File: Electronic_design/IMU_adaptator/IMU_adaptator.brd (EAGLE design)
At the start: 47.7 x 34.1 mm, 5 parts, among them J1 CLM-110-02-XX-D

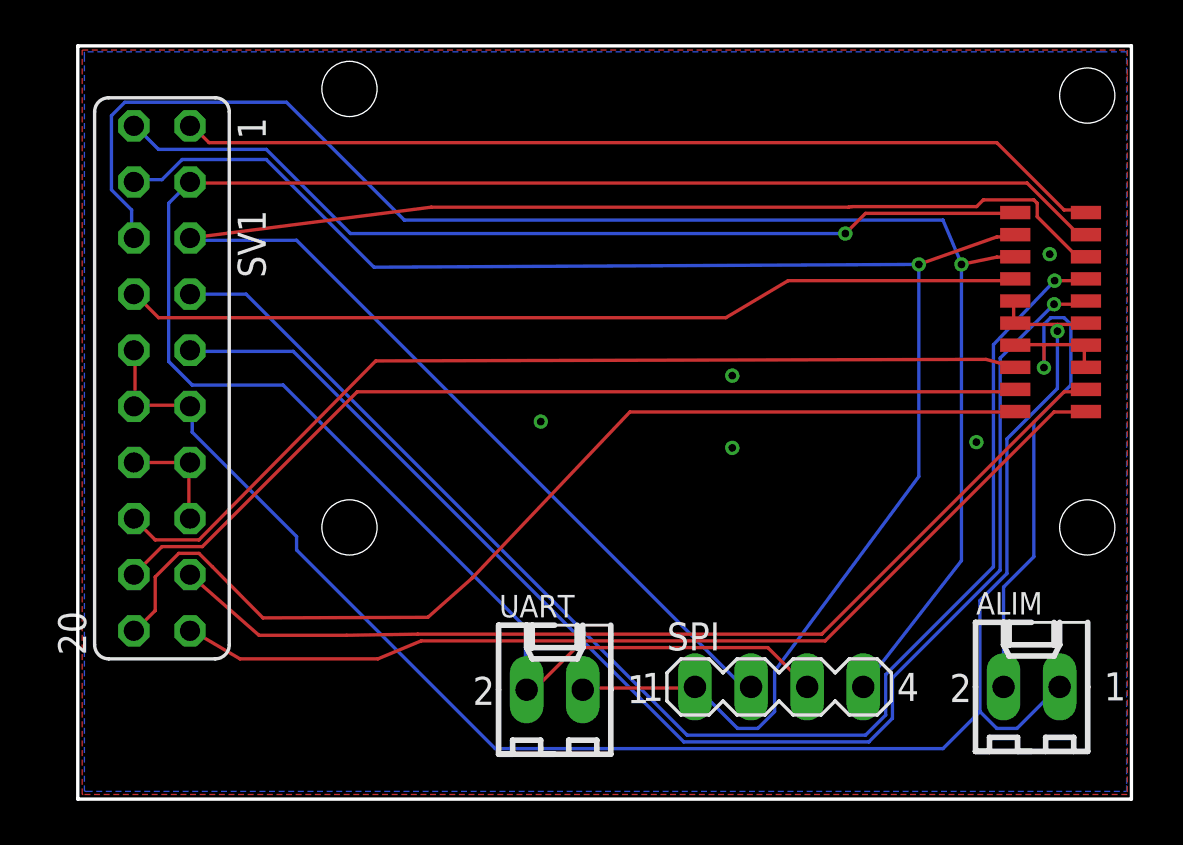
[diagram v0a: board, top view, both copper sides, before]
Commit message: reroutage carte IMU et STEPPER
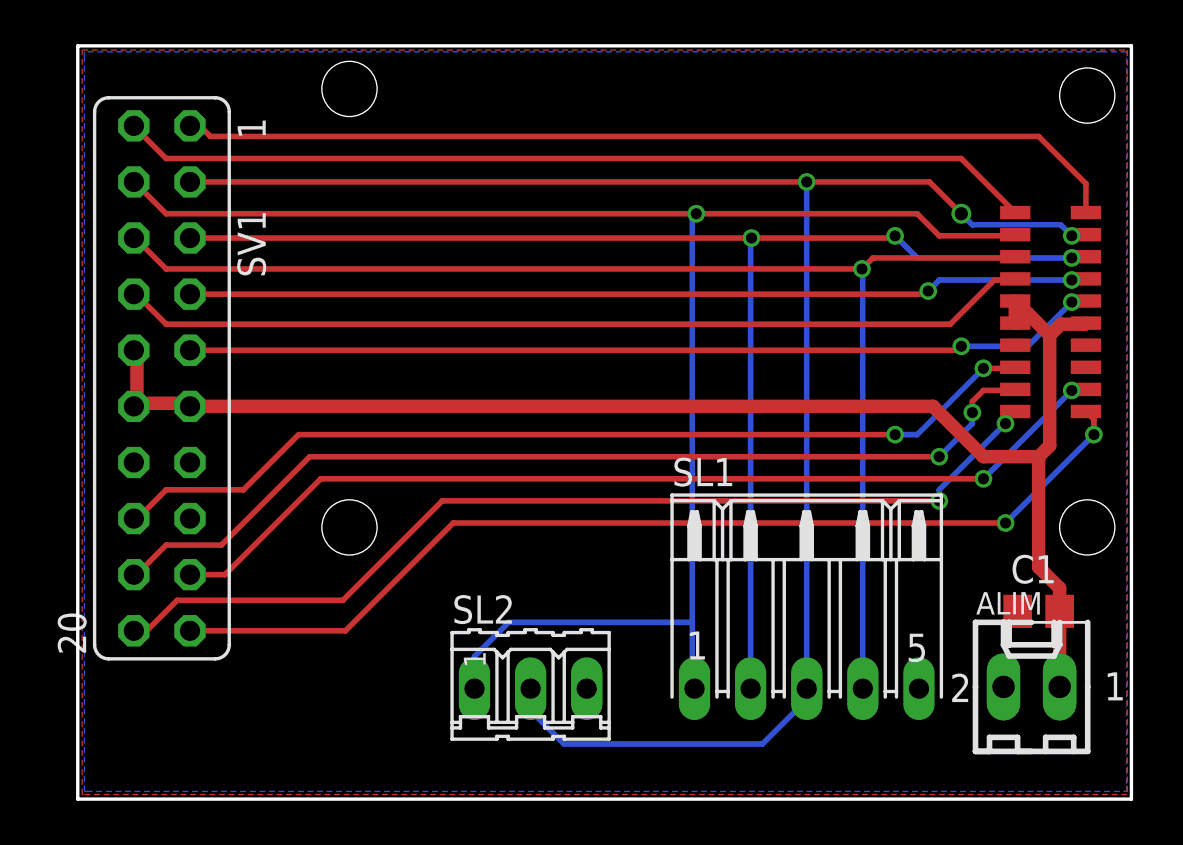
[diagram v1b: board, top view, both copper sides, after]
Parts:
- removed SPI: (no value), con-lstb:MA04-1
- removed UART: 22-27-2021-02, con-molex:6410-02
- added C1: (no value), eagle-ltspice:C0805
- added SL1: (no value), con-amp-quick:05PA
- added SL2: (no value), con-amp-quick:03P
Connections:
- net GND: now also C1.1, SL1.5, SL2.3
- net MISO/RX: now also SL1.1, SL2.1; no longer SPI.1, UART.1
- net MOSI: now also SL1.2; no longer SPI.2
- net SLCK/TX: now also SL1.3, SL2.2; no longer SPI.3, UART.2
- net SS: now also SL1.4; no longer SPI.4
- net VCC: now also C1.2
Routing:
- net GND: track 31.5 -> 0.00 mm, vias 6 -> 0
- net N$8: track 64.4 -> 40.8 mm, vias 1 -> 2
- net N$9: track 62.9 -> 41.5 mm, vias 1 -> 2
- net MOSI: track 76.1 -> 61.5 mm, vias 0 -> 3
- net SS: track 71.4 -> 59.8 mm
- net VCC: track 76.9 -> 66.0 mm, vias 1 -> 0
- net SLCK/TX: track 88.3 -> 80.1 mm, vias 0 -> 3
- net N$20: track 47.4 -> 44.4 mm, vias 0 -> 2
- net N$13: track 46.2 -> 44.0 mm, vias 0 -> 2
- net N$18: track 43.7 -> 42.7 mm, vias 0 -> 2
- net N$2: track 42.3 -> 41.5 mm, vias 1 -> 0
- net N$1: track 42.2 -> 43.0 mm
- net N$19: track 43.4 -> 44.0 mm, vias 0 -> 2
- net N$14: track 45.4 -> 45.8 mm, vias 0 -> 2
